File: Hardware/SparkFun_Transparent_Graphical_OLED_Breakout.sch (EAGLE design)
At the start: 39 parts, among them U1 AP3012, U2 UG-2856KLBAG01_4WSPI

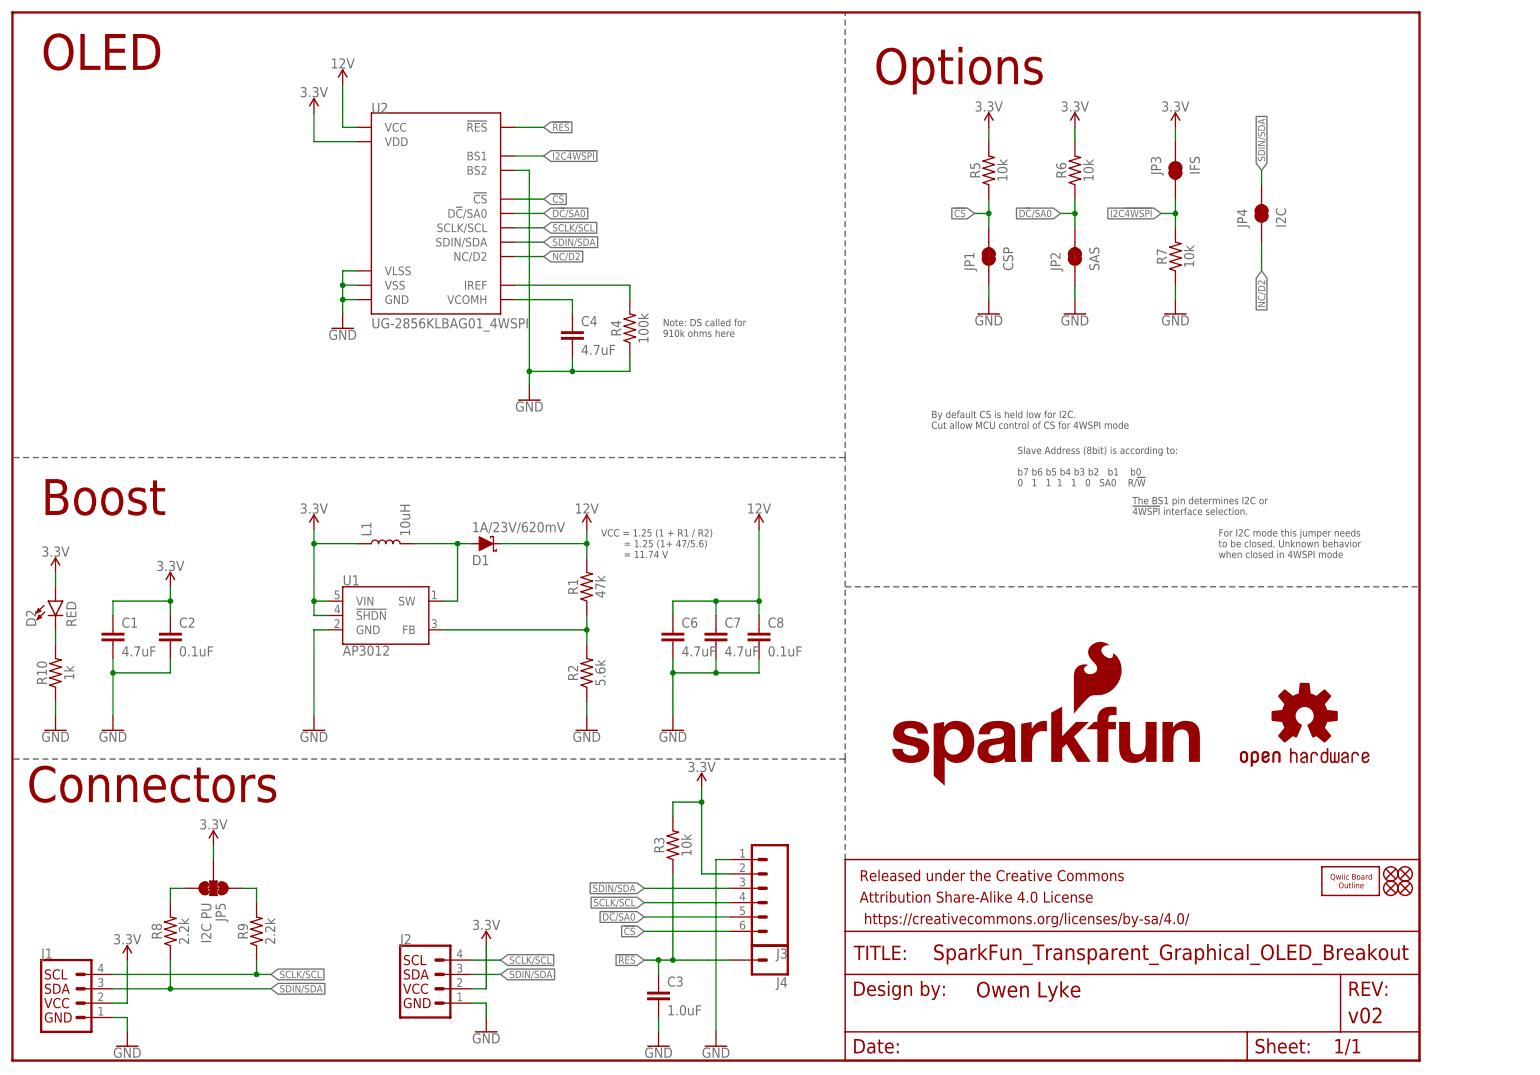
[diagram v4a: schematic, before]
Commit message: Notes from reds review added in board
Yeah its not standard, but it worked
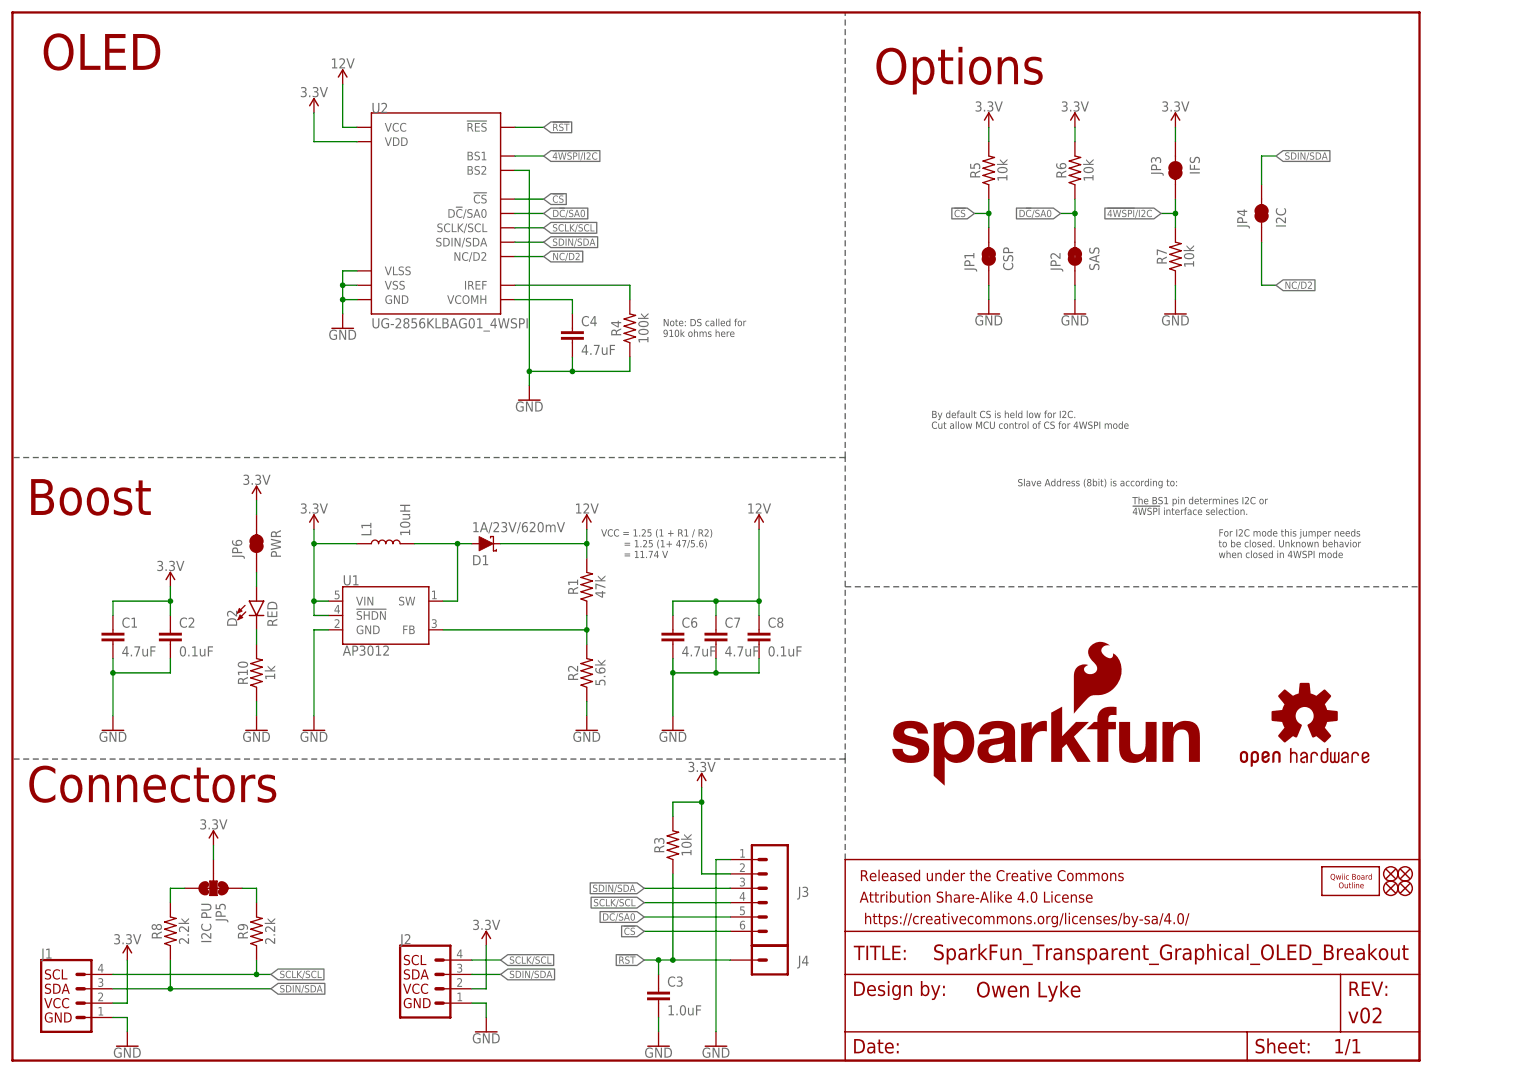
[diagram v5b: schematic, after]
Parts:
- added JP6: PWR, SparkFun-Jumpers:JUMPER-SMT_2_NC_TRACE_SILK
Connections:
- net !RES renamed !RST
- net I2C!4WSPI renamed !4WSPI!/I2C
- new net N$8: D2.A, JP6.1
- net 3.3V: now also JP6.2; no longer D2.A
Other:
- note added: "Slave Address (8bit) is according to:"
- note removed: "Slave Address (8bit) is according to: b7 b6 b5 b4 b3 b2 b1 b0 0 1 1 1 1 0 SA0 R/!W"
- moved on the sheet: D2, R10

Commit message: Fixed design review notes
Jumper labels simplified
FPC polarity markers added
version number updated
I2C resistors moved
test point added for 12V
LED disconnect jumper added
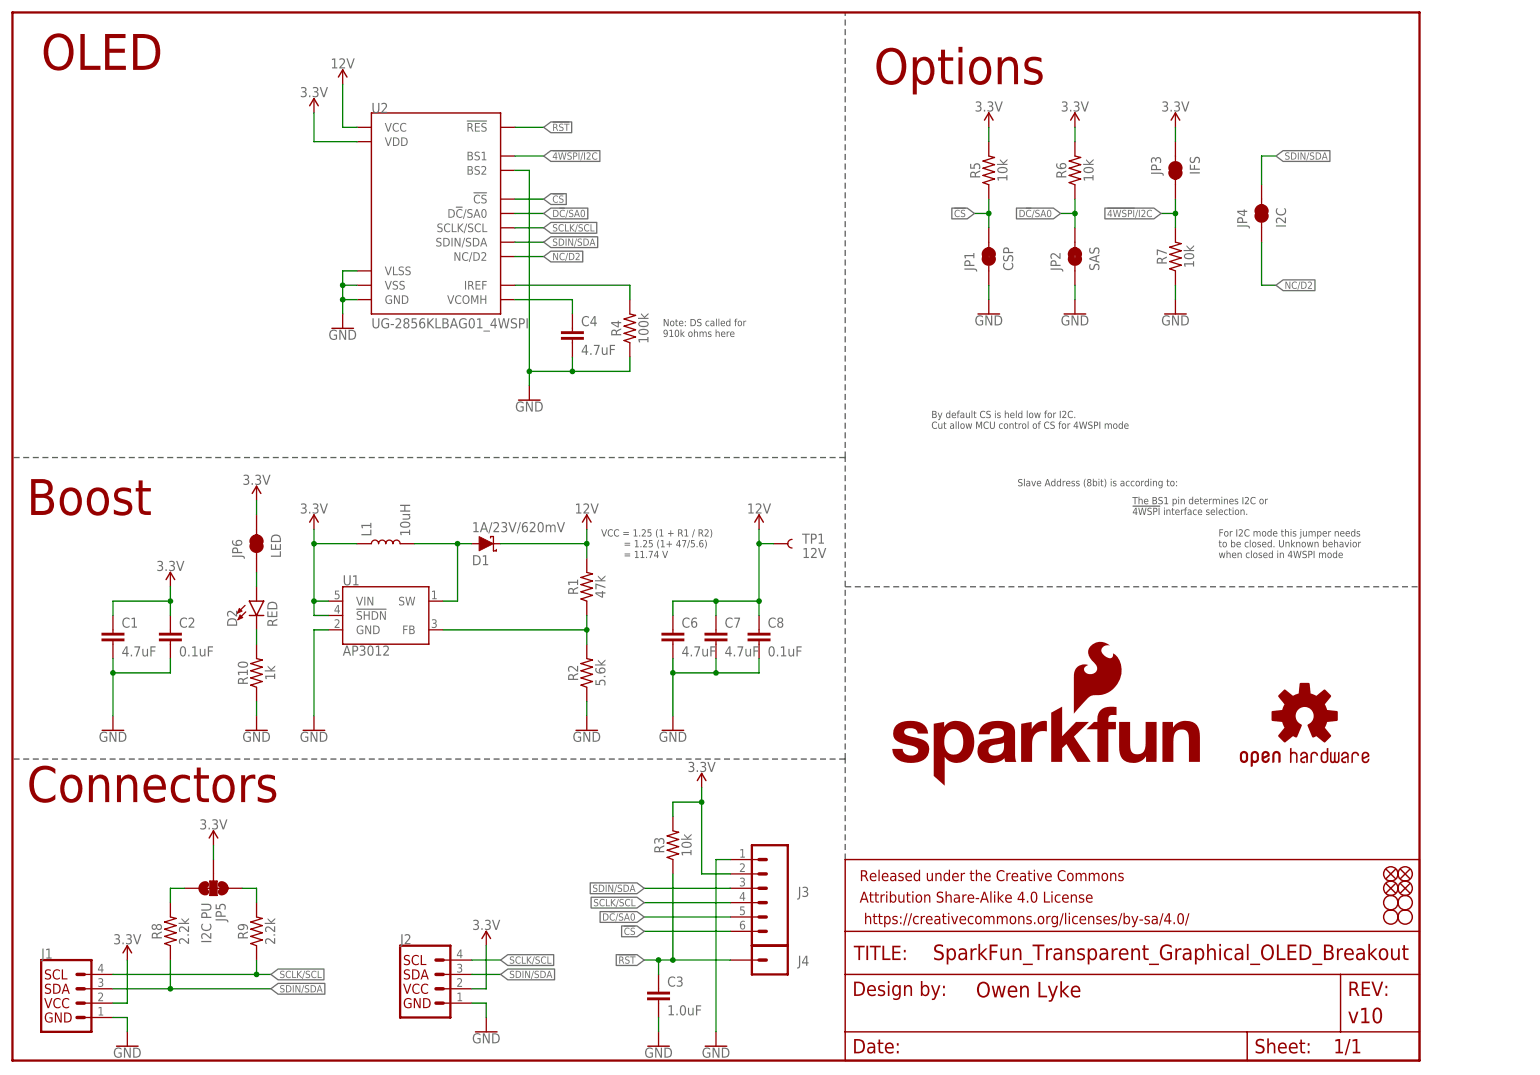
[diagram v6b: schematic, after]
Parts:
- removed U$1: QWIIC_BOARD_OUTLINEH, SparkX:QWIIC_BOARD_OUTLINEH
- added H1, H2, H3, H4: STAND-OFF, SparkFun-Hardware:STAND-OFF
- added TP1: 12V, SparkFun-Connectors:TEST-POINT3
- FRAME1: REV v02 -> v10
- JP6: value PWR -> LED
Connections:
- net 12V: now also TP1.1
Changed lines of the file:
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@@
 <?xml version="1.0" encoding="utf-8"?>
 <!DOCTYPE eagle SYSTEM "eagle.dtd">
-<eagle version="9.2.0">
+<eagle version="9.1.3">
 <drawing>
 <settings>
-<setting alwaysvectorfont="no"/>
+<setting alwaysvectorfont="yes"/>
 <setting verticaltext="up"/>
 </settings>
@@
 <part name="FRAME1" library="SparkFun-Aesthetics" deviceset="FRAME-LETTER" device="">
 <attribute name="DESIGNER" value="Owen Lyke"/>
-<attribute name="REV" value="v02"/>
+<attribute name="REV" value="v10"/>
 </part>
 <part name="J1" library="SparkFun-Connectors" deviceset="QWIIC_CONNECTOR" device="JS-1MM"/>
@@
 <part name="R3" library="SparkFun-Resistors" deviceset="10KOHM" device="-0603-1/10W-1%" value="10k"/>
 <part name="J4" library="SparkFun-Connectors" deviceset="CONN_01" device="PTH_NO_SILK_YES_STOP"/>
-<part name="U$1" library="SparkX" deviceset="QWIIC_BOARD_OUTLINE" device="H"/>
 <part name="LOGO1" library="SparkFun-Aesthetics" deviceset="SFE_LOGO_NAME_FLAME" device=".1_INCH"/>
 <part name="R8" library="SparkFun-Resistors" deviceset="2.2KOHM" device="-0603-1/10W-1%" value="2.2k"/>
@@
 <part name="R10" library="SparkFun-Resistors" deviceset="1KOHM" device="-0603-1/10W-1%" value="1k"/>
 <part name="JP5" library="SparkFun-Jumpers" deviceset="JUMPER-SMT_3_2-NC_TRACE" device="_SILK" value="I2C PU"/>
-<part name="JP6" library="SparkFun-Jumpers" deviceset="JUMPER-SMT_2_NC_TRACE" device="_SILK" value="PWR"/>
+<part name="JP6" library="SparkFun-Jumpers" deviceset="JUMPER-SMT_2_NC_TRACE" device="_SILK" value="LED"/>
+<part name="H1" library="SparkFun-Hardware" deviceset="STAND-OFF" device=""/>
+<part name="H2" library="SparkFun-Hardware" deviceset="STAND-OFF" device=""/>
+<part name="H3" library="SparkFun-Hardware" deviceset="STAND-OFF" device=""/>
+<part name="H4" library="SparkFun-Hardware" deviceset="STAND-OFF" device=""/>
+<part name="TP1" library="SparkFun-Connectors" deviceset="TEST-POINT" device="3" value="12V"/>
 </parts>
 <sheets>
@@
 <attribute name="NAME" x="140.97" y="18.542" size="1.778" layer="95" font="vector" rot="R180"/>
 </instance>
-<instance part="U$1" gate="G$1" x="236.728" y="31.75"/>
 <instance part="LOGO1" gate="G$1" x="154.94" y="48.26"/>
 <instance part="R8" gate="G$1" x="27.94" y="22.86" rot="R90">
@@
 <attribute name="NAME" x="40.64" y="88.9" size="1.778" layer="95" font="vector" rot="R90"/>
 <attribute name="VALUE" x="45.72" y="88.9" size="1.778" layer="96" font="vector" rot="R90" align="top-left"/>
+</instance>
+<instance part="H1" gate="G$1" x="243.84" y="27.94"/>
+<instance part="H2" gate="G$1" x="243.84" y="25.4"/>
+<instance part="H3" gate="G$1" x="246.38" y="25.4"/>
+<instance part="H4" gate="G$1" x="246.38" y="27.94"/>
+<instance part="TP1" gate="G$1" x="134.62" y="91.44" smashed="yes">
+<attribute name="NAME" x="139.7" y="91.44" size="1.778" layer="95" font="vector"/>
+<attribute name="VALUE" x="139.7" y="88.9" size="1.778" layer="96" font="vector"/>
 </instance>
 </instances>
@@
 <wire x1="116.84" y1="81.28" x2="124.46" y2="81.28" width="0.1524" layer="91"/>
 <wire x1="124.46" y1="81.28" x2="132.08" y2="81.28" width="0.1524" layer="91"/>
-<wire x1="132.08" y1="81.28" x2="132.08" y2="93.98" width="0.1524" layer="91"/>
+<wire x1="132.08" y1="81.28" x2="132.08" y2="91.44" width="0.1524" layer="91"/>
 <pinref part="C8" gate="G$1" pin="1"/>
+<wire x1="132.08" y1="91.44" x2="132.08" y2="93.98" width="0.1524" layer="91"/>
 <wire x1="132.08" y1="78.74" x2="132.08" y2="81.28" width="0.1524" layer="91"/>
 <junction x="132.08" y="81.28"/>
@@
 <junction x="124.46" y="81.28"/>
 <pinref part="SUPPLY9" gate="G$1" pin="12V"/>
-</segment>
-<segment>
+<pinref part="TP1" gate="G$1" pin="1"/>
+<wire x1="134.62" y1="91.44" x2="132.08" y2="91.44" width="0.1524" layer="91"/>
+<junction x="132.08" y="91.44"/>
+</segment>
+<segment>

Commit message: Minor changes from Checklist run-through
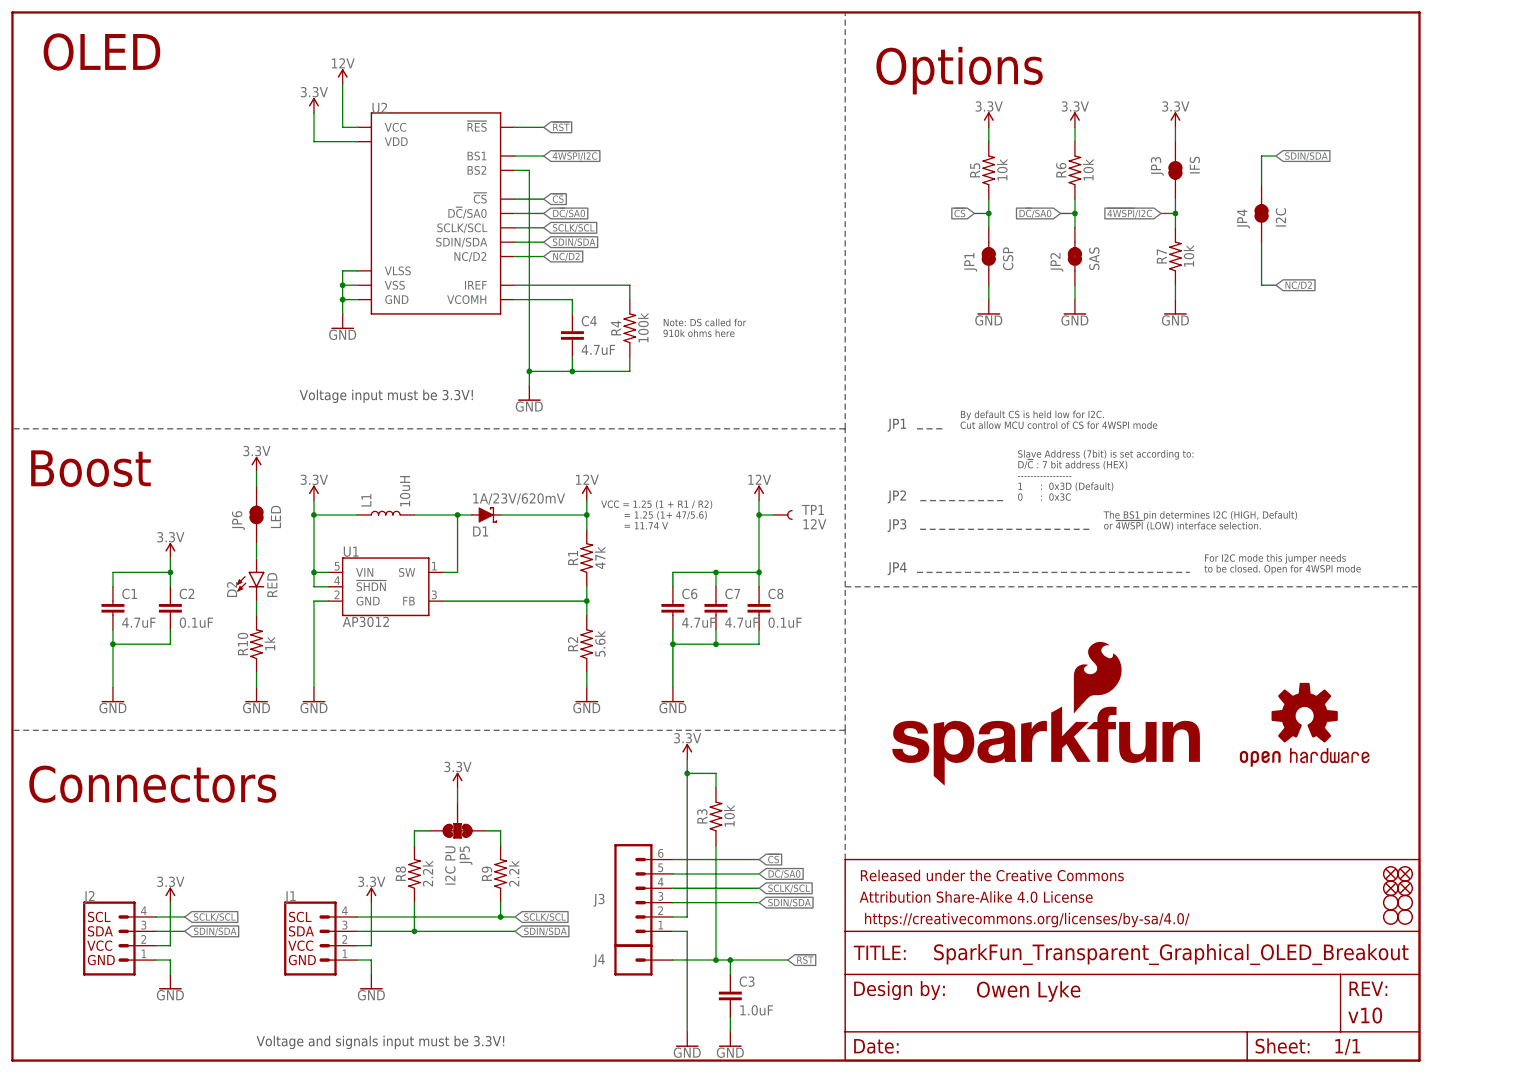
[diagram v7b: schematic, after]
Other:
- note added: "For I2C mode this jumper needs to be closed. Open for 4WSPI mode"
- note added: "JP1"
- note added: "JP2"
- note added: "JP3"
- note added: "JP4"
- note added: "Slave Address (7bit) is set according to: D/!C! : 7 bit address (HEX) ----------------- 1 : 0x3D (Default) 0 : 0x3C"
- note added: "The BS1 pin determines I2C (HIGH, Default) or !4WSPI! (LOW) interface selection."
- note added: "Voltage and signals input must be 3.3V!"
- note added: "Voltage input must be 3.3V!"
- note removed: "For I2C mode this jumper needs to be closed. Unknown behavior when closed in 4WSPI mode"
- note removed: "Slave Address (8bit) is according to:"
- note removed: "The BS1 pin determines I2C or !4WSPI! interface selection."
- moved on the sheet: C1, C2, C3, C6, C7, C8, D1, D2, J1, J2, J3, J4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

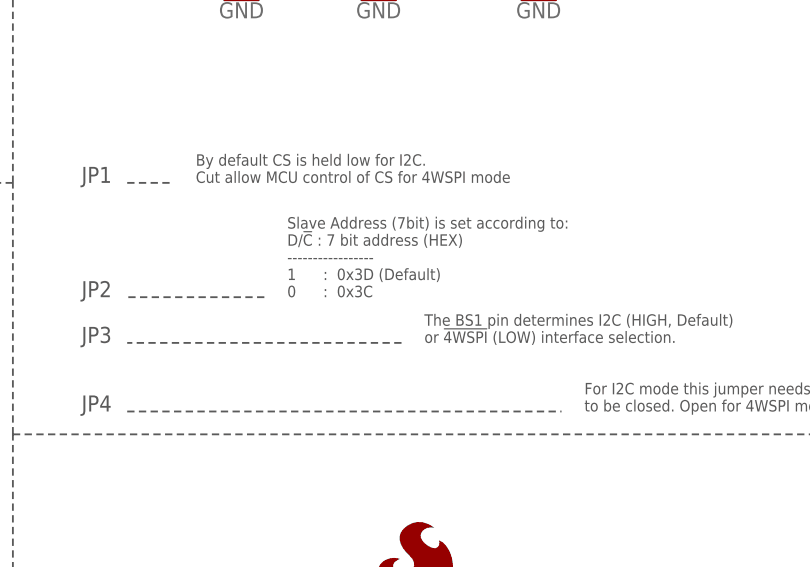
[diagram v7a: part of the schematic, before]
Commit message: Fix default label of I2C address in schematic
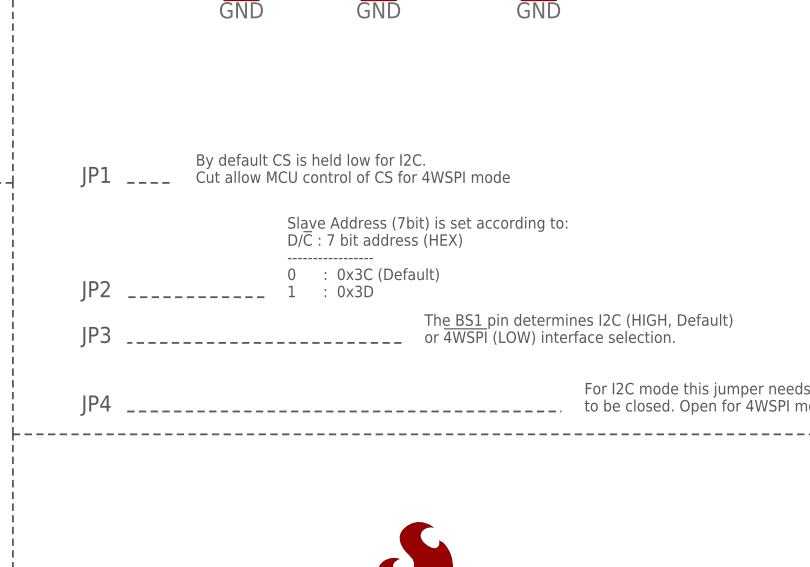
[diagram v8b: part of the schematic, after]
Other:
- note added: "Slave Address (7bit) is set according to: D/!C! : 7 bit address (HEX) ----------------- 0 : 0x3C (Default) 1 : 0x3D"
- note removed: "Slave Address (7bit) is set according to: D/!C! : 7 bit address (HEX) ----------------- 1 : 0x3D (Default) 0 : 0x3C"
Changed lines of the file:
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@@
 D/!C! : 7 bit address (HEX)
 -----------------
-1      :  0x3D (Default)
-0      :  0x3C</text>
+0      :  0x3C (Default)
+1      :  0x3D </text>
 <text x="193.04" y="93.98" size="1.27" layer="97">The BS1 pin determines I2C (HIGH, Default)
 or !4WSPI! (LOW) interface selection. </text>
